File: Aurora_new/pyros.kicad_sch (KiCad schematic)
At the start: 20 parts, among them J10 Screw_Terminal_01x02, J11 Screw_Terminal_01x02, J12 Screw_Terminal_01x04, J13 Screw_Terminal_01x02, J14 Screw_Terminal_01x02, J15 Screw_Terminal_01x02, J2 Screw_Terminal_01x04, J22 Screw_Terminal_01x08, J23 Screw_Terminal_01x08, J24 Screw_Terminal_01x08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

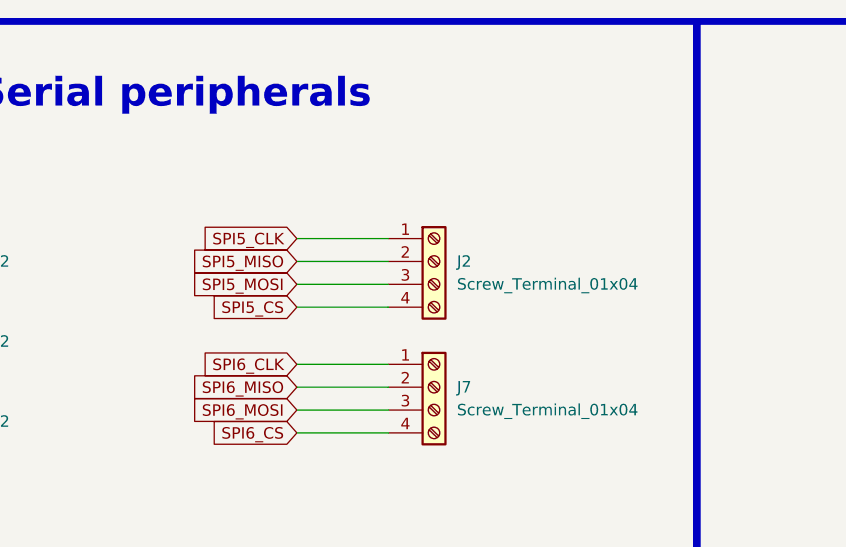
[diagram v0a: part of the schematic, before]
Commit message: layout and changed screw term size
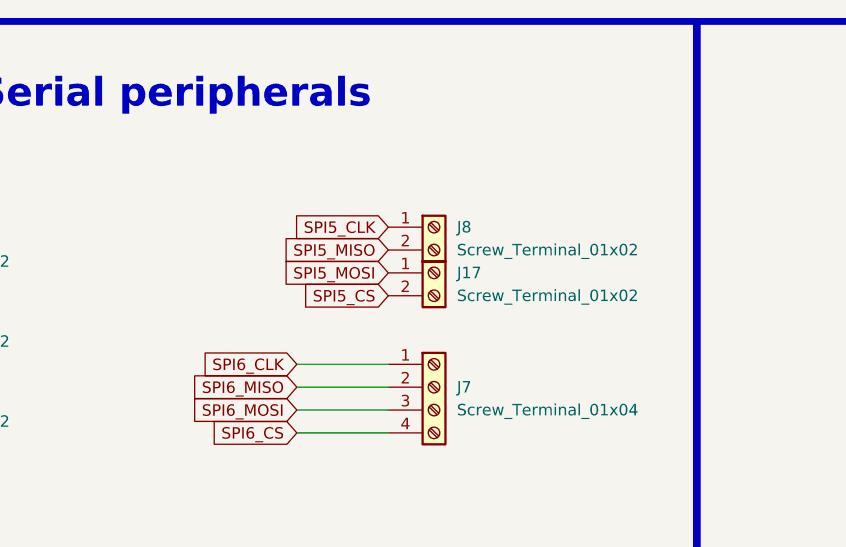
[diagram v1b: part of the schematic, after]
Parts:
- removed J2: Screw_Terminal_01x04, 1984633:PHOENIX_1984633, symbol Connector:Screw_Terminal_01x04
- added J17, J8: Screw_Terminal_01x02, 1984617:PHOENIX_1984617, symbol Connector:Screw_Terminal_01x02
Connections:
- net SPI5_CLK: now also J8.1 (Pin_1)
- net SPI5_CS: now also J17.2 (Pin_2)
- net SPI5_MISO: now also J8.2 (Pin_2)
- net SPI5_MOSI: now also J17.1 (Pin_1)
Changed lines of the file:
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@@
 	(wire
 		(pts
-			(xy 241.3 41.91) (xy 251.46 41.91)
-		)
-		(stroke
-			(width 0)
-			(type default)
-		)
-	)
-	(wire
-		(pts
 			(xy 368.3 66.04) (xy 363.22 66.04)
 		)
@@
 	(wire
 		(pts
-			(xy 241.3 44.45) (xy 251.46 44.45)
-		)
-		(stroke
-			(width 0)
-			(type default)
-		)
-	)
-	(wire
-		(pts
 			(xy 49.53 148.59) (xy 58.42 148.59)
 		)
@@
 	(wire
 		(pts
-			(xy 241.3 36.83) (xy 251.46 36.83)
-		)
-		(stroke
-			(width 0)
-			(type default)
-		)
-	)
-	(wire
-		(pts
 			(xy 49.53 156.21) (xy 58.42 156.21)
 		)
@@
 	(wire
 		(pts
-			(xy 241.3 39.37) (xy 251.46 39.37)
-		)
-		(stroke
-			(width 0)
-			(type default)
-		)
-	)
-	(wire
-		(pts
 			(xy 165.1 134.62) (xy 165.1 132.08)
 		)
@@
 	(global_label "SPI5_MOSI"
 		(shape input)
-		(at 241.3 41.91 180)
+		(at 251.46 40.64 180)
 		(fields_autoplaced yes)
 		(effects
@@
 		)
 		(property "Intersheetrefs" "${INTERSHEET_REFS}"
-			(at 228.4572 41.91 0)
+			(at 238.6172 40.64 0)
 			(effects
 				(font
@@
 	(global_label "SPI5_CS"
 		(shape input)
-		(at 241.3 44.45 180)
+		(at 251.46 43.18 180)
 		(fields_autoplaced yes)
 		(effects
@@
 		)
 		(property "Intersheetrefs" "${INTERSHEET_REFS}"
-			(at 230.5739 44.45 0)
+			(at 240.7339 43.18 0)
 			(effects
 				(font
@@
 	(global_label "SPI5_CLK"
 		(shape input)
-		(at 241.3 36.83 180)
+		(at 251.46 35.56 180)
 		(fields_autoplaced yes)
 		(effects
@@
 		)
 		(property "Intersheetrefs" "${INTERSHEET_REFS}"
-			(at 229.4853 36.83 0)
+			(at 239.6453 35.56 0)
 			(effects
 				(font
@@
 	(global_label "SPI5_MISO"
 		(shape input)
-		(at 241.3 39.37 180)
+		(at 251.46 38.1 180)
 		(fields_autoplaced yes)
 		(effects
@@
 		)
 		(property "Intersheetrefs" "${INTERSHEET_REFS}"
-			(at 228.4572 39.37 0)
+			(at 238.6172 38.1 0)
 			(effects
 				(font
@@
 	)
 	(symbol
+		(lib_id "Connector:Screw_Terminal_01x02")
+		(at 256.54 35.56 0)
+		(unit 1)
+		(exclude_from_sim no)
+		(in_bom yes)
+		(on_board yes)
+		(dnp no)
+		(fields_autoplaced yes)
+		(property "Reference" "J8"
+			(at 259.08 35.5599 0)
+			(effects
+				(font
+					(size 1.27 1.27)
+				)
+				(justify left)
+			)
+		)
+		(property "Value" "Screw_Terminal_01x02"
+			(at 259.08 38.0999 0)
+			(effects
+				(font
+					(size 1.27 1.27)
+				)
+				(justify left)
+			)
+		)
+		(property "Footprint" "1984617:PHOENIX_1984617"
+			(at 256.54 35.56 0)
+			(effects
+				(font
+					(size 1.27 1.27)
+				)
+				(hide yes)
+			)
+		)
+		(property "Datasheet" "~"
+			(at 256.54 35.56 0)
+			(effects
+				(font
+					(size 1.27 1.27)
+				)
+				(hide yes)
+			)
+		)
+		(property "Description" "Generic screw terminal, single row, 01x02, script generated (kicad-library-utils/schlib/autogen/connector/)"
+			(at 256.54 35.56 0)
+			(effects
+				(font
+					(size 1.27 1.27)
+				)
+				(hide yes)
+			)
+		)
+		(property "PURCHASE-URL" "https://www.digikey.com/en/products/detail/phoenix-contact/1729128/260615?msockid=2519f0312b83673a161fe62a2a5a66c9"
+			(at 256.54 35.56 0)
+			(effects
+				(font
+					(size 1.27 1.27)
+				)
+				(hide yes)
+			)
+		)
+		(property "Price" " $1.33000"
+			(at 256.54 35.56 0)
+			(effects
+				(font
+					(size 1.27 1.27)
+				)
+				(hide yes)
+			)
+		)
+		(pin "2"
+		)
+		(pin "1"
+		)
+		(instances
+			(project "Aurora"
+				(path "/073f53a3-faa8-4419-bff2-f325850469a4/b243e184-8694-4e24-9f49-14da58e669df"
+					(reference "J8")
+					(unit 1)
+				)
+			)
+		)
+	)
+	(symbol
 		(lib_id "power:GND")
 		(at 337.82 48.26 0)
@@
 	(symbol
 		(lib_id "Connector:Screw_Terminal_01x04")
-		(at 256.54 39.37 0)
-		(unit 1)
-		(exclude_from_sim no)
-		(in_bom yes)
-		(on_board yes)
-		(dnp no)
-		(fields_autoplaced yes)
-		(property "Reference" "J2"
-			(at 259.08 39.3699 0)
-			(effects
-				(font
-					(size 1.27 1.27)
-				)
-				(justify left)
-			)
-		)
-		(property "Value" "Screw_Terminal_01x04"
-			(at 259.08 41.9099 0)
-			(effects
-				(font
-					(size 1.27 1.27)
-				)
-				(justify left)
-			)
-		)
-		(property "Footprint" "1984633:PHOENIX_1984633"
-			(at 256.54 39.37 0)
-			(effects
-				(font
-					(size 1.27 1.27)
-				)
-				(hide yes)
-			)
-		)
-		(property "Datasheet" "~"
-			(at 256.54 39.37 0)
-			(effects
-				(font
-					(size 1.27 1.27)
-				)
-				(hide yes)
-			)
-		)
-		(property "Description" "Generic screw terminal, single row, 01x04, script generated (kicad-library-utils/schlib/autogen/connector/)"
-			(at 256.54 39.37 0)
-			(effects
-				(font
-					(size 1.27 1.27)
-				)
-				(hide yes)
-			)
-		)
-		(property "PURCHASE-URL" "https://www.digikey.com/en/products/detail/phoenix-contact/1715747/260633"
-			(at 256.54 39.37 0)
-			(effects
-				(font
-					(size 1.27 1.27)
-				)
-				(hide yes)
-			)
-		)
-		(property "Price" " $2.06500"
-			(at 256.54 39.37 0)
-			(effects
-				(font
-					(size 1.27 1.27)
-				)
-				(hide yes)
-			)
-		)
-		(pin "2"
-		)
-		(pin "3"
-		)
-		(pin "4"
-		)
-		(pin "1"
-		)
-		(instances
-			(project ""
-				(path "/073f53a3-faa8-4419-bff2-f325850469a4/b243e184-8694-4e24-9f49-14da58e669df"
-					(reference "J2")
-					(unit 1)
-				)
-			)
-		)
-	)
-	(symbol
-		(lib_id "Connector:Screw_Terminal_01x04")
 		(at 186.69 76.2 0)
 		(unit 1)
@@
 					(unit 1)
 				)
+			)
+		)
+	)
+	(symbol
+		(lib_id "Connector:Screw_Terminal_01x02")
+		(at 256.54 40.64 0)
+		(unit 1)
+		(exclude_from_sim no)
+		(in_bom yes)
+		(on_board yes)
+		(dnp no)
+		(fields_autoplaced yes)
+		(property "Reference" "J17"
+			(at 259.08 40.6399 0)
+			(effects
+				(font
+					(size 1.27 1.27)
+				)
+				(justify left)
+			)
+		)
+		(property "Value" "Screw_Terminal_01x02"
+			(at 259.08 43.1799 0)
+			(effects
+				(font
+					(size 1.27 1.27)
+				)
+				(justify left)
+			)
+		)
+		(property "Footprint" "1984617:PHOENIX_1984617"
+			(at 256.54 40.64 0)
+			(effects
+				(font
+					(size 1.27 1.27)
+				)
+				(hide yes)
+			)
+		)
+		(property "Datasheet" "~"
+			(at 256.54 40.64 0)
+			(effects
+				(font
+					(size 1.27 1.27)
+				)
+				(hide yes)
+			)
+		)
+		(property "Description" "Generic screw terminal, single row, 01x02, script generated (kicad-library-utils/schlib/autogen/connector/)"
+			(at 256.54 40.64 0)
+			(effects
+				(font
+					(size 1.27 1.27)
+				)
+				(hide yes)
+			)
+		)
+		(property "PURCHASE-URL" "https://www.digikey.com/en/products/detail/phoenix-contact/1729128/260615?msockid=2519f0312b83673a161fe62a2a5a66c9"
+			(at 256.54 40.64 0)
+			(effects
+				(font
+					(size 1.27 1.27)
+				)
+				(hide yes)
+			)
+		)
+		(property "Price" " $1.33000"
+			(at 256.54 40.64 0)
+			(effects
+				(font
+					(size 1.27 1.27)
+				)
+				(hide yes)
+			)
+		)
+		(pin "2"
+		)
+		(pin "1"
+		)
+		(instances
+			(project "Aurora"
+				(path "/073f53a3-faa8-4419-bff2-f325850469a4/b243e184-8694-4e24-9f49-14da58e669df"
+					(reference "J17")
+					(unit 1)
+				)

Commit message: changing a lot of stuff, like components and footprints
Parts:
- J10, J11, J13, J14, J15, J17, J8: footprint 1984617:PHOENIX_1984617 -> 1725656:PHOENIX_1725656
- J12, J33, J34, J35, J7, J9: footprint 1984633:PHOENIX_1984633 -> 1725672:PHOENIX_1725672
- J22, J23, J24, J25, J4, J5: footprint 1984675:PHOENIX_1984675 -> 1725711:PHOENIX_1725711
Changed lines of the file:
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@@
 			)
 		)
-		(property "Footprint" "1984633:PHOENIX_1984633"
+		(property "Footprint" "1725672:PHOENIX_1725672"
 			(at 256.54 53.34 0)
 			(effects
@@
 		)
 		(property "Price" " $2.06500"
+			(at 256.54 53.34 0)
+			(effects
+				(font
+					(size 1.27 1.27)
+				)
+				(hide yes)
+			)
+		)
+		(property "DigiKey_Part_Number" ""
 			(at 256.54 53.34 0)
 			(effects
@@
 			)
 		)
-		(property "Footprint" "1984633:PHOENIX_1984633"
+		(property "Footprint" "1725672:PHOENIX_1725672"
 			(at 176.53 148.59 0)
 			(effects
@@
 		)
 		(property "Price" " $2.06500"
+			(at 176.53 148.59 0)
+			(effects
+				(font
+					(size 1.27 1.27)
+				)
+				(hide yes)
+			)
+		)
+		(property "DigiKey_Part_Number" ""
 			(at 176.53 148.59 0)
 			(effects
@@
 			)
 		)
-		(property "Footprint" "1984675:PHOENIX_1984675"
+		(property "Footprint" "1725711:PHOENIX_1725711"
 			(at 63.5 60.96 0)
 			(effects
@@
 		)
 		(property "Price" " $4.07700"
+			(at 63.5 60.96 0)
+			(effects
+				(font
+					(size 1.27 1.27)
+				)
+				(hide yes)
+			)
+		)
+		(property "DigiKey_Part_Number" ""
 			(at 63.5 60.96 0)
 			(effects
@@
 			)
 		)
-		(property "Footprint" "1984617:PHOENIX_1984617"
+		(property "Footprint" "1725656:PHOENIX_1725656"
 			(at 256.54 35.56 0)
 			(effects
@@
 		)
 		(property "Price" " $1.33000"
+			(at 256.54 35.56 0)
+			(effects
+				(font
+					(size 1.27 1.27)
+				)
+				(hide yes)
+			)
+		)
+		(property "DigiKey_Part_Number" ""
 			(at 256.54 35.56 0)
 			(effects
@@
 			)
 		)
-		(property "Footprint" "1984675:PHOENIX_1984675"
+		(property "Footprint" "1725711:PHOENIX_1725711"
 			(at 63.5 179.07 0)
 			(effects
@@
 		)
 		(property "Price" " $4.07700"
+			(at 63.5 179.07 0)
+			(effects
+				(font
+					(size 1.27 1.27)
+				)
+				(hide yes)
+			)
+		)
+		(property "DigiKey_Part_Number" ""
 			(at 63.5 179.07 0)
 			(effects
@@
 			)
 		)
-		(property "Footprint" "1984617:PHOENIX_1984617"
+		(property "Footprint" "1725656:PHOENIX_1725656"
 			(at 186.69 54.61 0)
 			(effects
@@
 		)
 		(property "Price" " $1.33000"
+			(at 186.69 54.61 0)
+			(effects
+				(font
+					(size 1.27 1.27)
+				)
+				(hide yes)
+			)
+		)
+		(property "DigiKey_Part_Number" ""
 			(at 186.69 54.61 0)
 			(effects
@@
 			)
 		)
-		(property "Footprint" "1984633:PHOENIX_1984633"
+		(property "Footprint" "1725672:PHOENIX_1725672"
 			(at 186.69 76.2 0)
 			(effects
@@
 		)
 		(property "Price" " $2.06500"
+			(at 186.69 76.2 0)
+			(effects
+				(font
+					(size 1.27 1.27)
+				)
+				(hide yes)
+			)
+		)
+		(property "DigiKey_Part_Number" ""
 			(at 186.69 76.2 0)
 			(effects
@@
 			)
 		)
+		(property "DigiKey_Part_Number" ""
+			(at 346.71 41.91 0)
+			(effects
+				(font
+					(size 1.27 1.27)
+				)
+				(hide yes)
+			)
+		)
 		(pin "1"
 		)
@@
 			)
 		)
-		(property "Footprint" "1984675:PHOENIX_1984675"
+		(property "Footprint" "1725711:PHOENIX_1725711"
 			(at 63.5 115.57 0)
 			(effects
@@
 		)
 		(property "Price" " $4.07700"
+			(at 63.5 115.57 0)
+			(effects
+				(font
+					(size 1.27 1.27)
+				)
+				(hide yes)
+			)
+		)
+		(property "DigiKey_Part_Number" ""
 			(at 63.5 115.57 0)
 			(effects
@@
 			)
 		)
-		(property "Footprint" "1984617:PHOENIX_1984617"
+		(property "Footprint" "1725656:PHOENIX_1725656"
 			(at 186.69 36.83 0)
 			(effects
@@
 		)
 		(property "Price" " $1.33000"
+			(at 186.69 36.83 0)
+			(effects
+				(font
+					(size 1.27 1.27)
+				)
+				(hide yes)
+			)
+		)
+		(property "DigiKey_Part_Number" ""
 			(at 186.69 36.83 0)
 			(effects
@@
 			)
 		)
-		(property "Footprint" "1984675:PHOENIX_1984675"
+		(property "Footprint" "1725711:PHOENIX_1725711"
 			(at 63.5 151.13 0)
 			(effects
@@
 		)
 		(property "Price" " $4.07700"
+			(at 63.5 151.13 0)
+			(effects
+				(font
+					(size 1.27 1.27)
+				)
+				(hide yes)
+			)
+		)
+		(property "DigiKey_Part_Number" ""
 			(at 63.5 151.13 0)
 			(effects
@@
 			)
 		)
+		(property "DigiKey_Part_Number" ""
+			(at 350.52 66.04 0)
+			(effects
+				(font
+					(size 1.27 1.27)
+				)
+				(hide yes)
+			)
+		)
 		(pin "2"
 		)
@@
 			)
 		)
-		(property "Footprint" "1984617:PHOENIX_1984617"
+		(property "Footprint" "1725656:PHOENIX_1725656"
 			(at 256.54 92.71 0)
 			(effects
@@
 		)
 		(property "Price" " $1.33000"
+			(at 256.54 92.71 0)
+			(effects
+				(font
+					(size 1.27 1.27)
+				)
+				(hide yes)
+			)
+		)
+		(property "DigiKey_Part_Number" ""
 			(at 256.54 92.71 0)
 			(effects
@@
 			)
 		)
-		(property "Footprint" "1984633:PHOENIX_1984633"
+		(property "Footprint" "1725672:PHOENIX_1725672"
 			(at 186.69 90.17 0)
 			(effects
@@
 		)
 		(property "Price" " $2.06500"
+			(at 186.69 90.17 0)
+			(effects
+				(font
+					(size 1.27 1.27)
+				)
+				(hide yes)
+			)
+		)
+		(property "DigiKey_Part_Number" ""
 			(at 186.69 90.17 0)
 			(effects
@@
 			)
 		)
-		(property "Footprint" "1984617:PHOENIX_1984617"
+		(property "Footprint" "1725656:PHOENIX_1725656"
 			(at 256.54 40.64 0)
 			(effects
@@
 		)
 		(property "Price" " $1.33000"
+			(at 256.54 40.64 0)
+			(effects
+				(font
+					(size 1.27 1.27)
+				)
+				(hide yes)
+			)
+		)
+		(property "DigiKey_Part_Number" ""
 			(at 256.54 40.64 0)
 			(effects
@@
 			)
 		)
-		(property "Footprint" "1984633:PHOENIX_1984633"
+		(property "Footprint" "1725672:PHOENIX_1725672"
 			(at 176.53 132.08 0)
 			(effects
@@
 		)
 		(property "Price" " $2.06500"
+			(at 176.53 132.08 0)
+			(effects
+				(font
+					(size 1.27 1.27)
+				)
+				(hide yes)
+			)
+		)
+		(property "DigiKey_Part_Number" ""
 			(at 176.53 132.08 0)
 			(effects
@@
 			)
 		)
-		(property "Footprint" "1984675:PHOENIX_1984675"
+		(property "Footprint" "1725711:PHOENIX_1725711"
 			(at 63.5 86.36 0)
 			(effects
@@
 		)
 		(property "Price" " $4.07700"
+			(at 63.5 86.36 0)
+			(effects
+				(font
+					(size 1.27 1.27)
+				)
+				(hide yes)
+			)
+		)
+		(property "DigiKey_Part_Number" ""
 			(at 63.5 86.36 0)
 			(effects
@@
 			)
 		)
-		(property "Footprint" "1984675:PHOENIX_1984675"
+		(property "Footprint" "1725711:PHOENIX_1725711"
 			(at 63.5 35.56 0)
 			(effects
@@
 		)
 		(property "Price" " $4.07700"
+			(at 63.5 35.56 0)
+			(effects
+				(font
+					(size 1.27 1.27)
+				)
+				(hide yes)
+			)
+		)
+		(property "DigiKey_Part_Number" ""
 			(at 63.5 35.56 0)
 			(effects
@@
 			)
 		)
-		(property "Footprint" "1984617:PHOENIX_1984617"
+		(property "Footprint" "1725656:PHOENIX_1725656"
 			(at 256.54 83.82 0)
 			(effects
@@
 		)
 		(property "Price" " $1.33000"
+			(at 256.54 83.82 0)
+			(effects
+				(font
+					(size 1.27 1.27)
+				)
+				(hide yes)
+			)
+		)
+		(property "DigiKey_Part_Number" ""
 			(at 256.54 83.82 0)
 			(effects
@@
 			)
 		)
-		(property "Footprint" "1984617:PHOENIX_1984617"
+		(property "Footprint" "1725656:PHOENIX_1725656"
 			(at 186.69 45.72 0)
 			(effects
@@
 		)
 		(property "Price" " $1.33000"
+			(at 186.69 45.72 0)
+			(effects
+				(font
+					(size 1.27 1.27)
+				)
+				(hide yes)
+			)
+		)
+		(property "DigiKey_Part_Number" ""
 			(at 186.69 45.72 0)
 			(effects
@@
 			)
 		)
-		(property "Footprint" "1984633:PHOENIX_1984633"
+		(property "Footprint" "1725672:PHOENIX_1725672"
 			(at 218.44 139.7 0)
 			(effects
@@
 			(at 218.44 139.7 0)
 			(effects
+				(font
+					(size 1.27 1.27)
+				)
+				(hide yes)
+			)
+		)
+		(property "DigiKey_Part_Number" ""
+			(at 218.44 139.7 0)
+			(effects
